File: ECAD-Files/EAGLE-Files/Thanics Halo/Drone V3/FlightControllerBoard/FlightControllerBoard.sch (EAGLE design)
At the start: 92 parts, among them J12 UE27AE54100, J4 UE27AE54100, J5 U.FL, J7 62674-301121ALF, J8 MICROSD, U3 MPL115A2, U4 NEO-M8, U5 VL53L1

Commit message: Finished overall board zoning and component placement
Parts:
- removed C19, C22, C7, C8: 16pF, 16pF-capacitor:GRM1555C1H160JA01DG-155-M
- removed J6: (no value), thanics_robotics:JST_SH_2POS
- removed R32: 20R, 20-resistor:RC0603JR-0720RLRC0603N-M
- removed U5: VL53L1, thanics_robotics:VL53L1
- added C1, C12: 0.1uF, 0.1uF-capacitor-0402:0402ZD104KAT2A0402-M
- added D2, D3, D4: GREEN, SparkFun-LED:LED-GREEN0603
- added J10, J11, J15, J16, J17, J18, J19, J20, J21, J22, J9: (no value), thanics_robotics:JST_SH_4POS
- added JP1: (no value), pinhead:PINHD-2X6
- added L4: 1000R, 600ohm-fb:BLM18AG601SN1DIND_BLM18_0603-M
- added R24, R25, R26, R27: 49R9, 49.9-resistor:RC0402FR-0749K9LRC0402N-M
- added R28, R30, R31: 1k, 1k-resistor:RC0603JR-071KLRC0603N-M
- added R29: 10k, 10k-resistor(0603):RC0603JR-0710KLRC0603N-M
- C41: value 0.1uF -> 22uF; device 0.1uF-capacitor-0402:0402ZD104KAT2A0402-M -> 22uF X5R Ceramic Capacitor:GRM21BR60J226ME39L
- C42: value 4.7uF -> 10uF; device 4.7uF-capacitor:06036D475KAT2A0603-M -> 10uF X5R Ceramic Capacitor:GRM21BR60J106ME19L
- R10, R11, R13, R14, R2: device 10k-resistor:ERA-6AEB103V -> 10k-resistor(0603):RC0603JR-0710KLRC0603N-M
- R19: value 10k -> 1k; device 10k-resistor:ERA-6AEB103V -> 1k-resistor:RC0603JR-071KLRC0603N-M
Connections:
- removed net BATT_SCL: J7.2020
- removed net BATT_SDA: J7.1919
- removed net GPCLK: U2A.XI
- removed net N$17: U6.GPIO37
- new net ETH_BIAS: C1.2, L4.2, U$1.ETH_BIAS
- new net GND1: D2.C, U$1.LINK_LED_LAN
- new net GND2: D3.C
- new net GPIO12: JP1.1, U6.GPIO12
- new net GPIO13: JP1.3, U6.GPIO13
- new net GPIO16: JP1.5, U6.GPIO16
- new net GPIO17: JP1.2, U6.GPIO17
- new net GPIO37: JP1.4, U6.GPIO37
- new net GPIO38: JP1.6, U6.GPIO38
- new net GPIO39: JP1.8, U6.GPIO39
- new net N$22: D3.A, R30.11
- new net N$23: C12.2, L4.1, R24.11, R25.11, R26.11, R27.11
- new net N$24: R2.22, U$1.CONFIG
- new net N$25: D4.A, U$1.CPU_STAT_LED
- new net N$27: D4.C, R31.11
- net +3V3: now also C42.11, J10.1, J11.1, J15.1, J16.1, J17.1, J18.1, J19.1, J20.1, J21.1, J22.1, J9.1, JP1.11, R19.22, R29.22, R30.22, U$1.VCC, U$1.VCC@2, U$2.!E, U$2.VCC; no longer C41.2, C42.2, R19.11, R2.22, R32.22, U5.AVDD, U5.AVDDVCSEL
- net +5V: now also C41.11, JP1.12, U$1.VRF, U$1.VRF@2; no longer J6.1
- net 3.3V_A: now also R2.11, R28.22
- net GND: now also C1.1, C12.1, C41.22, C42.22, J10.4, J11.4, J15.4, J16.4, J17.4, J18.4, J19.4, J20.4, J21.4, J22.4, J9.4, JP1.10, R31.22, U$1.GND, U$1.GND@2, U$1.GND@3, U$1.GND@4, U$1.GND@5, U$1.GND@6, U$2.GND; no longer C19.11, C22.11, C41.1, C42.1, C7.11, C8.11, J6.2, U5.AVSSVCSEL, U5.GND
- net GPCLK1: now also U2A.XI
- net I2C_SCL: now also J10.3, J11.3, J15.3, J16.3, J17.3, J18.3, J19.3, J20.3, J21.3, J22.3, J7.2020, J9.3, JP1.7; no longer U5.SCL
- net I2C_SDA: now also J10.2, J11.2, J15.2, J16.2, J17.2, J18.2, J19.2, J20.2, J21.2, J22.2, J7.1919, J9.2, JP1.9; no longer U5.SDA
- net N$12: now also D2.A, R28.11; no longer R19.22, U5.XSHUT
- net N$3: now also R29.11; no longer R2.11
- net N$4: now also R19.11; no longer R32.11
- net NRST: now also U$2.3Z
- net NRST1: now also U$2.3Y0
- net NRST2: now also U$2.3Y1
- net RX_LAN_N: now also R25.22
- net RX_LAN_P: now also R26.22
- net RX_N: no longer C7.22
- net RX_P: no longer C19.22
- net SEL2: now also U$2.S1, U$2.S2, U$2.S3
- net SWCLK: now also U$2.2Z
- net SWCLK1: now also U$2.2Y0
- net SWCLK2: now also U$2.2Y1
- net SWDIO: now also U$2.1Z
- net SWDIO1: now also U$2.1Y0
- net SWDIO2: now also U$2.1Y1
- net TX_LAN_N: now also R27.22
- net TX_LAN_P: now also R24.22
- net TX_N: no longer C22.22
- net TX_P: no longer C8.22
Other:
- note added: "LIDAR Connectors"
- note added: "Other Connectors"
- note removed: "Connectors"
- moved on the sheet: C2, C23, C3, C36, C37, C38, C41, C42, J3, J7, J8, R19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

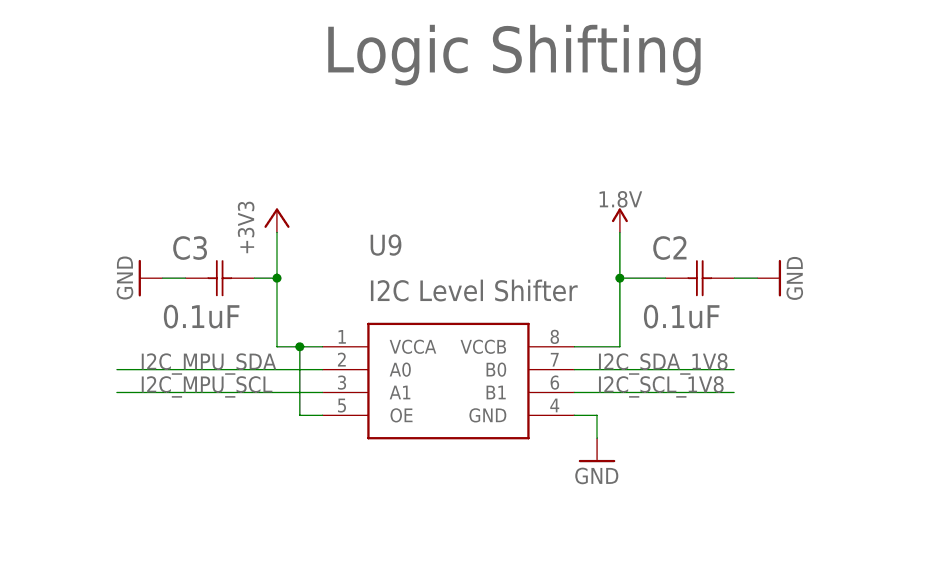
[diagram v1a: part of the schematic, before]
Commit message: Repositioned ethernet pullup resistors
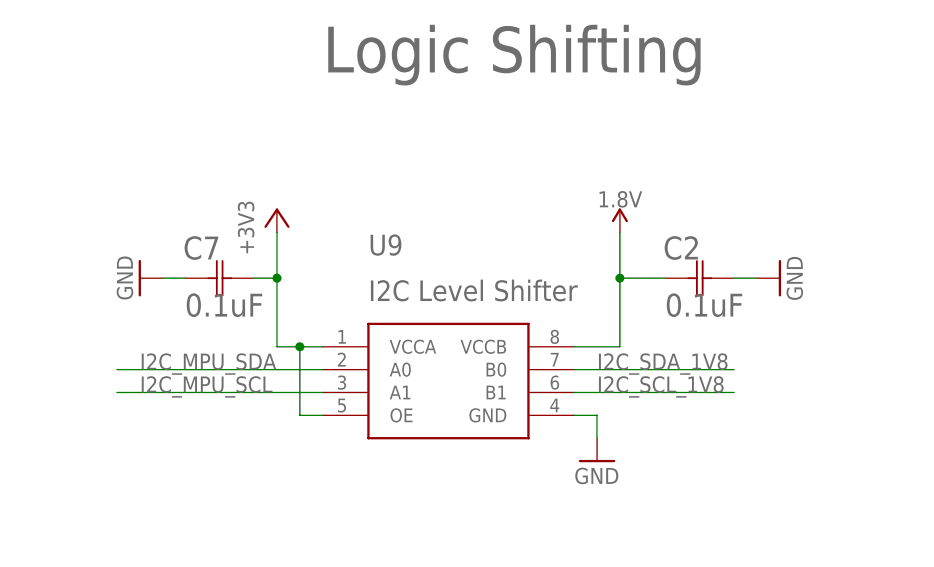
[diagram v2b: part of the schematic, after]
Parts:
- removed C3: 0.1uF, 0.1uF X7R Ceramic Capacitor:08055C104KAT2A
- added C7: 0.1uF, 0.1uF-capacitor-0402:0402ZD104KAT2A0402-M
- C2: device 0.1uF X7R Ceramic Capacitor:08055C104KAT2A -> 0.1uF-capacitor-0402:0402ZD104KAT2A0402-M
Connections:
- net +3V3: now also C7.2; no longer C3.2
- net GND: now also C7.1; no longer C3.1
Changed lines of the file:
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@@
 <part name="SUPPLY1" library="SparkFun-PowerSymbols" deviceset="1.8V" device=""/>
 <part name="SUPPLY2" library="SparkFun-PowerSymbols" deviceset="1.8V" device=""/>
-<part name="C2" library="0.1uF X7R Ceramic Capacitor" deviceset="08055C104KAT2A" device="" value="0.1uF"/>
 <part name="GND7" library="supply1" deviceset="GND" device=""/>
 <part name="GND9" library="supply1" deviceset="GND" device=""/>
 <part name="+3V7" library="supply1" deviceset="+3V3" device=""/>
 <part name="U9" library="thanics_robotics" deviceset="FXMAR2102" device=""/>
-<part name="C3" library="0.1uF X7R Ceramic Capacitor" deviceset="08055C104KAT2A" device="" value="0.1uF"/>
 <part name="GND10" library="supply1" deviceset="GND" device=""/>
 <part name="SUPPLY4" library="SparkFun-PowerSymbols" deviceset="1.8V" device=""/>
@@
 <part name="R29" library="10k-resistor(0603)" deviceset="RC0603JR-0710KL" device="RC0603N-M" value="10k"/>
 <part name="R14" library="10k-resistor(0603)" deviceset="RC0603JR-0710KL" device="RC0603N-M" value="10k"/>
+<part name="C7" library="0.1uF-capacitor-0402" deviceset="0402ZD104KAT2A" device="0402-M" value="0.1uF"/>
+<part name="C2" library="0.1uF-capacitor-0402" deviceset="0402ZD104KAT2A" device="0402-M" value="0.1uF"/>
 </parts>
 <sheets>
@@
 <instance part="SUPPLY1" gate="G$1" x="-43.18" y="-93.98"/>
 <instance part="SUPPLY2" gate="G$1" x="40.64" y="-93.98"/>
-<instance part="C2" gate="A" x="-198.12" y="-121.92"/>
 <instance part="GND7" gate="1" x="-205.74" y="-142.24"/>
 <instance part="GND9" gate="1" x="-256.54" y="-121.92" rot="R270"/>
 <instance part="+3V7" gate="G$1" x="-241.3" y="-114.3"/>
 <instance part="U9" gate="G$1" x="-228.6" y="-134.62"/>
-<instance part="C3" gate="A" x="-251.46" y="-121.92"/>
 <instance part="GND10" gate="1" x="-185.42" y="-121.92" rot="R90"/>
 <instance part="SUPPLY4" gate="G$1" x="-203.2" y="-116.84"/>
@@
 <instance part="R29" gate="A" x="393.7" y="15.24"/>
 <instance part="R14" gate="A" x="167.64" y="165.1"/>
+<instance part="C7" gate="A" x="-251.46" y="-121.92"/>
+<instance part="C2" gate="A" x="-198.12" y="-121.92"/>
 </instances>
 <busses>
@@
 <segment>
 <pinref part="GND9" gate="1" pin="GND"/>
-<pinref part="C3" gate="A" pin="1"/>
 <wire x1="-254" y1="-121.92" x2="-251.46" y2="-121.92" width="0.1524" layer="91"/>
-</segment>
-<segment>
-<pinref part="C2" gate="A" pin="2"/>
+<pinref part="C7" gate="A" pin="1"/>
+</segment>
+<segment>
 <pinref part="GND10" gate="1" pin="GND"/>
 <wire x1="-190.5" y1="-121.92" x2="-187.96" y2="-121.92" width="0.1524" layer="91"/>
+<pinref part="C2" gate="A" pin="2"/>
 </segment>
 <segment>
@@
 <wire x1="-238.76" y1="-137.16" x2="-238.76" y2="-129.54" width="0.1524" layer="91"/>
 <junction x="-238.76" y="-129.54"/>
-<pinref part="C3" gate="A" pin="2"/>
 <wire x1="-243.84" y1="-121.92" x2="-241.3" y2="-121.92" width="0.1524" layer="91"/>
 <junction x="-241.3" y="-121.92"/>
+<pinref part="C7" gate="A" pin="2"/>
 </segment>
 <segment>
@@
 <wire x1="-208.28" y1="-129.54" x2="-203.2" y2="-129.54" width="0.1524" layer="91"/>
 <wire x1="-203.2" y1="-129.54" x2="-203.2" y2="-121.92" width="0.1524" layer="91"/>
-<pinref part="C2" gate="A" pin="1"/>
 <wire x1="-203.2" y1="-121.92" x2="-203.2" y2="-116.84" width="0.1524" layer="91"/>
 <wire x1="-203.2" y1="-121.92" x2="-198.12" y2="-121.92" width="0.1524" layer="91"/>
 <junction x="-203.2" y="-121.92"/>
 <pinref part="SUPPLY4" gate="G$1" pin="1.8V"/>
-</segment>
-<segment>
+<pinref part="C2" gate="A" pin="1"/>
+</segment>
+<segment>

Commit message: Routed more traces, recognized that PowerSwitchingBoard connector needs to be reversed
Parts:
- removed D3: GREEN, SparkFun-LED:LED-GREEN0603
- removed JP1: (no value), pinhead:PINHD-2X6
- removed R11, R13: 10k, 10k-resistor(0603):RC0603JR-0710KLRC0603N-M
- removed R30: 1k, 1k-resistor:RC0603JR-071KLRC0603N-M
- removed R45: 10k, 10k-resistor:ERA-6AEB103V
- added R32: 10k, 10k-resistor(0603):RC0603JR-0710KLRC0603N-M
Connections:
- removed net GND2: D3.C
- removed net N$22: D3.A, R30.11
- net +3V3: now also R2.11; no longer JP1.11, R30.22
- net +5V: no longer JP1.12
- net 3.3V_A: no longer R2.11
- net GND: now also R32.22; no longer JP1.10, R11.22, R13.22, R45.22
- net GPIO12: no longer JP1.1
- net GPIO13: no longer JP1.3
- net GPIO16: no longer JP1.5
- net GPIO17: no longer JP1.2
- net GPIO37: no longer JP1.4
- net GPIO38: no longer JP1.6
- net GPIO39: no longer JP1.8
- net I2C_SCL: no longer JP1.7
- net I2C_SDA: no longer JP1.9
- net N$53: now also R32.11; no longer R45.11
- net SCL0: no longer R11.11
- net SDA0: no longer R13.11

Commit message: Finished Power Switching Board and Flight Controller Board v1
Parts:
- added JP1: (no value), pinhead:PINHD-1X1
- L4: value 1000R -> 1k@100MHz
- renumbered U$1 to U7, U$2 to U8
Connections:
- removed net FAULT: J7.2727
- net GEAR: now also JP1.1
- net GND: now also J7.2727

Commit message: Changed ethernet capacitor isolation to transformers
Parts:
- removed C23, C36, C37, C38: 0.1uF, 0.1uF-capacitor-0402:0402ZD104KAT2A0402-M
- added C3, C8: 0.1uF, 0.1uF-capacitor-0402:0402ZD104KAT2A0402-M
- added T1, T2: ALT4532M, thanics_robotics:ALT4532M
- R12: value 10 -> 10R
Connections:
- net BOOT0 renamed PWR_EN
- net +3V3: no longer U8.!E
- net 3.3V_A: now also C8.2, T1.3, T2.3
- net GND: now also C3.1, C8.1, U8.!E
- net N$23: now also C3.2, T1.6, T2.6
- net RX_LAN_N: now also R26.22, T1.1; no longer C36.2, R25.22
- net RX_LAN_P: now also R25.22, T1.2; no longer C23.2, R26.22
- net RX_N: now also R23.22, T1.5; no longer C36.1, R22.22
- net RX_P: now also R22.22, T1.4; no longer C23.1, R23.22
- net TX_LAN_N: now also T2.2; no longer C38.2
- net TX_LAN_P: now also T2.1; no longer C37.2
- net TX_N: now also T2.4; no longer C38.1
- net TX_P: now also T2.5; no longer C37.1
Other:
- moved on the sheet: C1, C12, C14, C15, C16, C17, C18, C20, C25, C26, C27, C28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
